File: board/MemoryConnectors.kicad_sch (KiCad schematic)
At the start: 7 parts, among them J29 Conn_02x18_Odd_Even, J30 Conn_02x18_Odd_Even, J31 Conn_02x18_Odd_Even, J32 Conn_02x18_Odd_Even, J33 Conn_02x18_Odd_Even, J34 Conn_02x18_Odd_Even, J35 Conn_02x18_Odd_Even

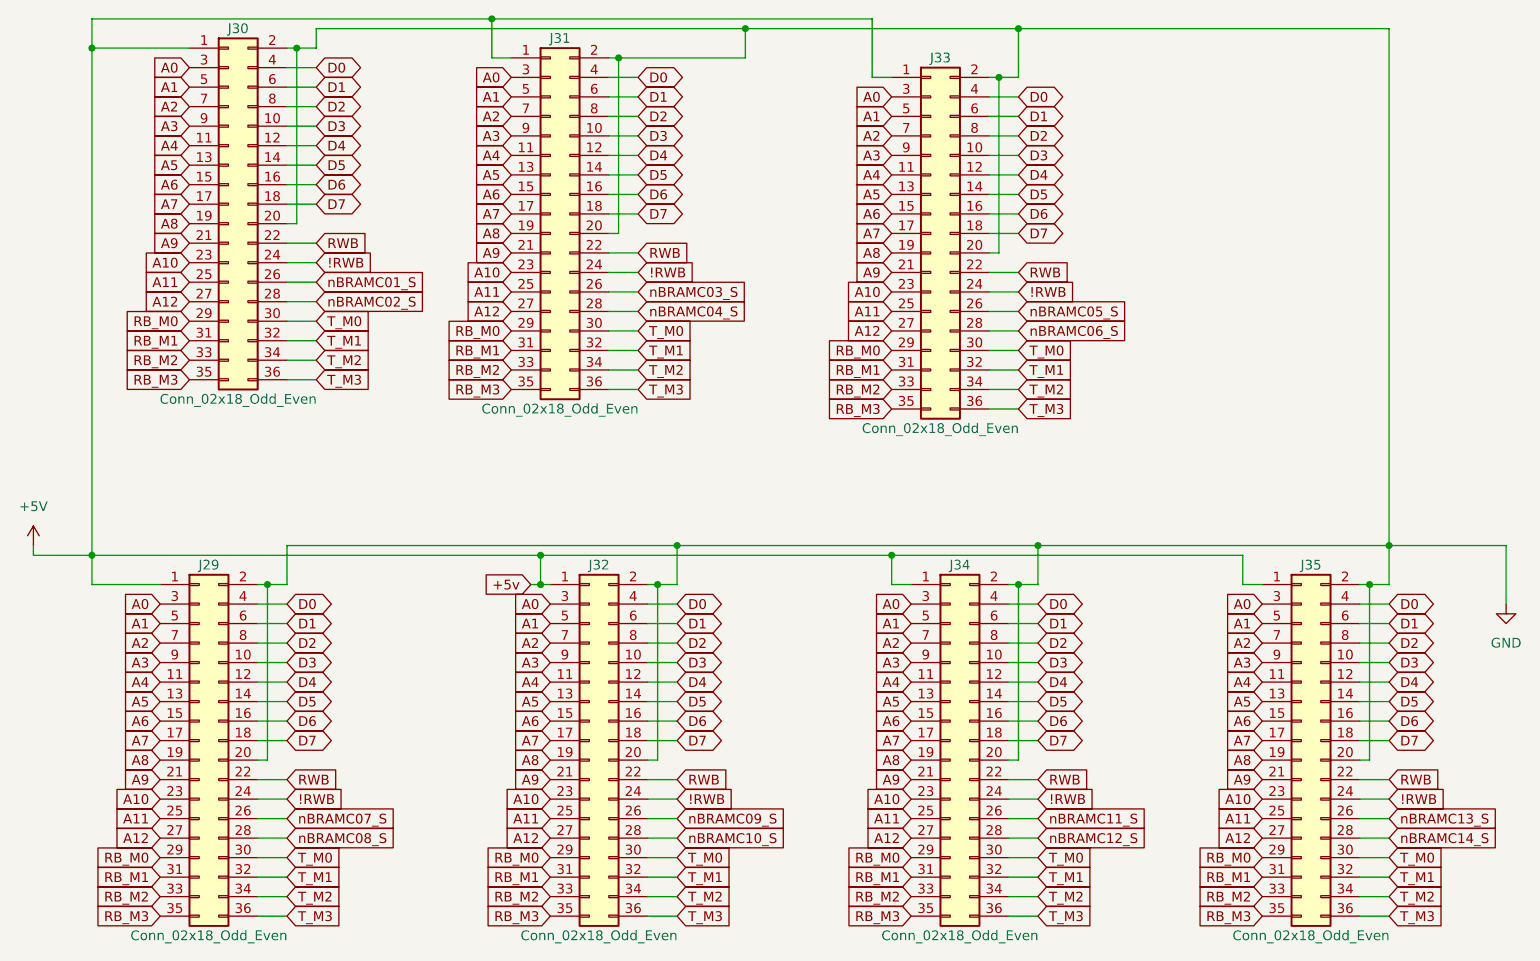
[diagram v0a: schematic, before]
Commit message: V2.0: wait states, GAL glue logic, serial clock and review fixes
Main board schematic:
- Replace the T4-T7 clock divider with RDY wait states. Fixed 7.16 MHz
  CPU clock; J36 selects 3.58 MHz for Rockwell parts. Waits are set per
  region through the write-only register at $FFF5 (reset = 3 waits).
- Move address decode, strobes, the wait-state generator, the IRQ
  encoder/latch/vector mux, ROM bank gating and DMA sync into seven GALs
  (U81-U86 ATF22V10C, U87 ATF16V8C), removing 29 ICs. CUPL sources,
  JEDECs and notes are in board/PLDs/V2.
- 1.8432 MHz serial clock, soft-power latch, -5V regulator, bulk caps,
  pull-ups, audio coupling/decoupling, GNDA tie, read-only Z register
  and other design-review fixes.
- New WaitStates and Support sheets; project symbol library
  hydra16.kicad_sym with sym-lib-table.

PCB updated from the schematic. Includes pending changes to the counter,
bus breakout and memory daughter card projects.

Firmware:
- Remove S_REGISTER; T/U/V/W now at $FFF0-$FFF3 to match the hardware.
- Add math.s and sound.s (included by os_main.s).
- Rebuild the 65C02 ROM image.

Co-Authored-By: Claude Opus 5.5 <noreply@anthropic.com>
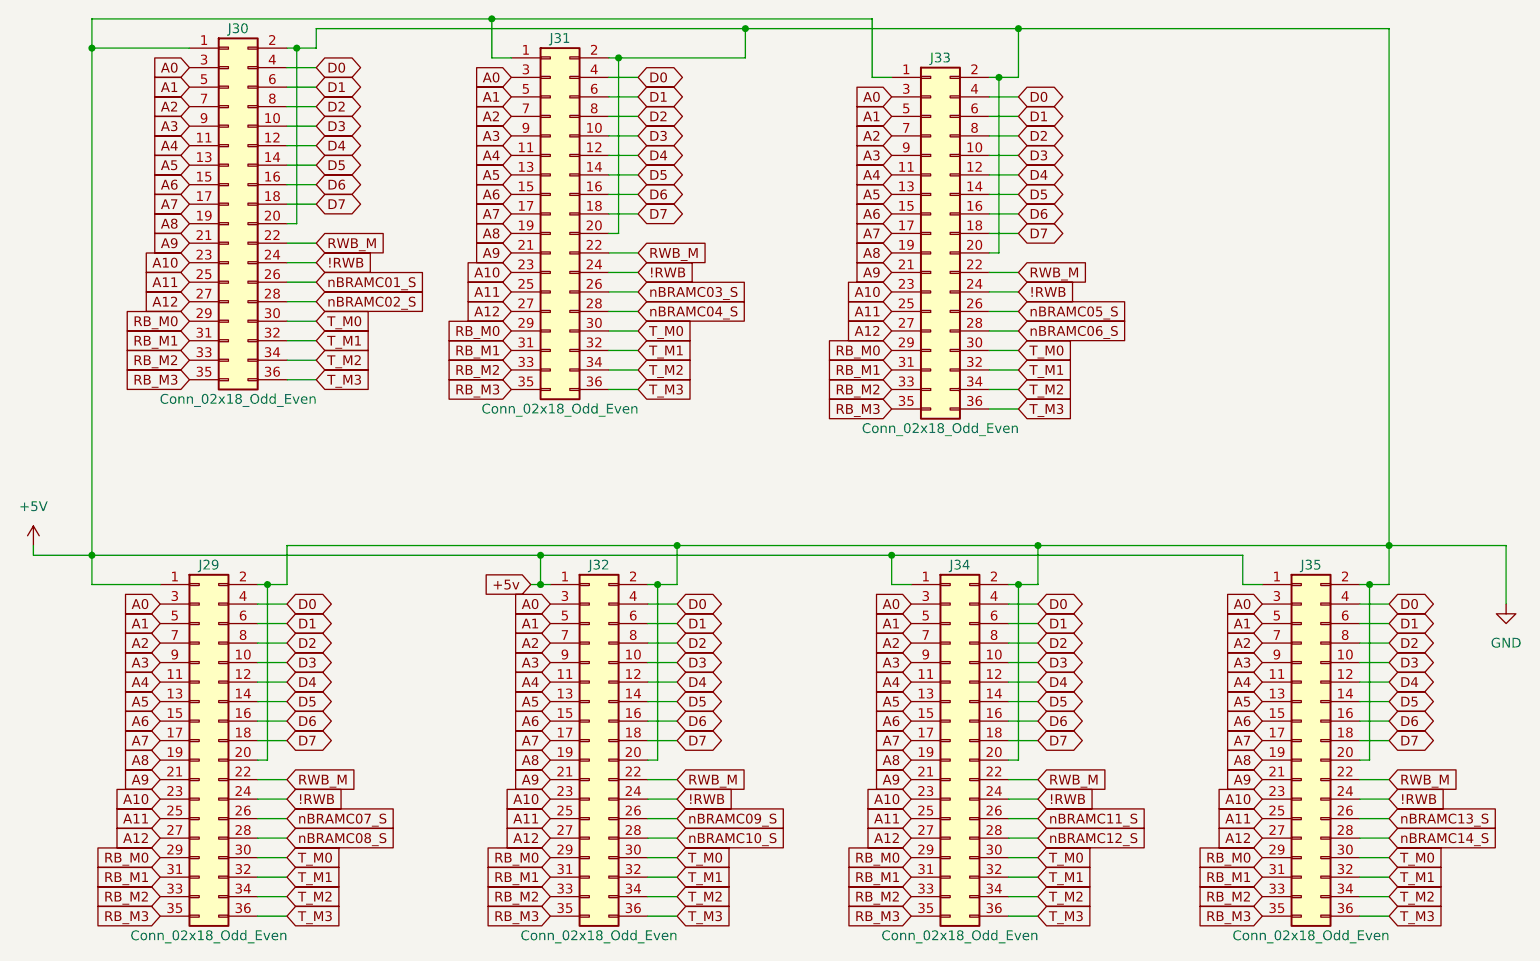
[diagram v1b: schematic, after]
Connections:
- net RWB renamed RWB_M
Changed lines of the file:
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@@
 		)
 	)
-	(global_label "RWB"
+	(global_label "RWB_M"
 		(shape input)
 		(at 113.03 66.04 0)
@@
 		)
 	)
-	(global_label "RWB"
+	(global_label "RWB_M"
 		(shape input)
 		(at 71.12 64.77 0)
@@
 		)
 	)
-	(global_label "RWB"
+	(global_label "RWB_M"
 		(shape input)
 		(at 210.82 134.62 0)
@@
 		)
 	)
-	(global_label "RWB"
+	(global_label "RWB_M"
 		(shape input)
 		(at 118.11 134.62 0)
@@
 		)
 	)
-	(global_label "RWB"
+	(global_label "RWB_M"
 		(shape input)
 		(at 162.56 68.58 0)
@@
 		)
 	)
-	(global_label "RWB"
+	(global_label "RWB_M"
 		(shape input)
 		(at 165.1 134.62 0)
@@
 		)
 	)
-	(global_label "RWB"
+	(global_label "RWB_M"
 		(shape input)
 		(at 67.31 134.62 0)

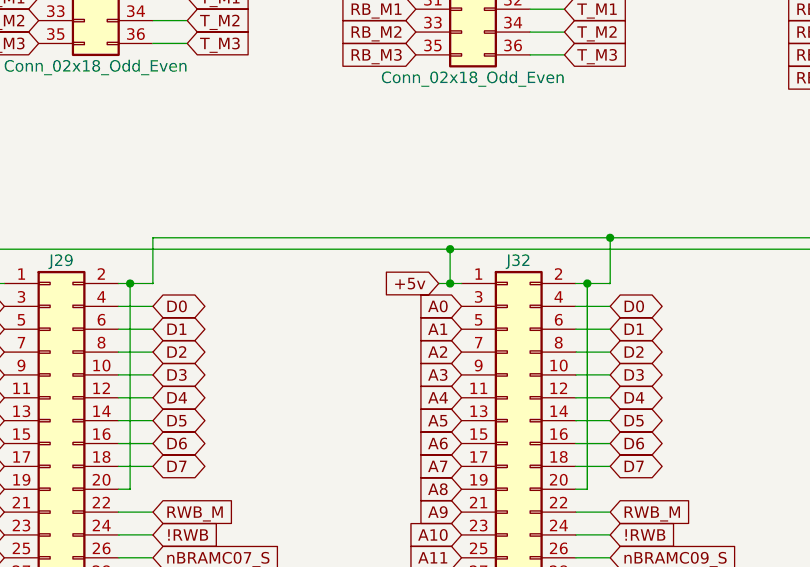
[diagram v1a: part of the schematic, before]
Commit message: V2.0 rev 2.0D: clock stretching, OS ROM paging and review fixes
Bus timing:
- New GAL C (U88) generates PHI2/PHI1 and the 3.58 MHz sound clock from
  the 14.318 MHz master, replacing the U35 74F191 divider. J36 now selects
  7.16 or 3.58 MHz.
- Banked RAM, banked ROM and slot I/O ($FF20-$FFEF) get one extra PHI2-low
  period plus 0-3 extra PHI2-high periods set in $FFF5 (GAL D). This
  replaces the on-board RDY wait generator; cards can still pull RDY.
- Write strobes are now hold-time safe: PHI1 comes straight from GAL C
  and RWB_M straight from GAL B2.

Review fixes:
- OS ROM chip enable from a single-level decode, output enable from
  GAL B1; -55 part specified. Full 4K OS ROM paging via GAL G.
- Vector RAM writes only during PHI2; $FFF0-$FFFF no longer slowed.
- YM2151 /WR on RWB_M. U62 removed. RB0-RB7 pull-ups (RN5).
- Slot clocks driven through U56 and U34 with 33R series resistors.
- J38 enables in-system flashing of the banked ROMs.
- W65C22S/W65C51N, AS6C4008, DS1813-5 and CY7C192-25 values; R4 1k.
- J7 pin 8 no longer +5V; +5VA renamed +5VSB; serial handshake loop.
- Sheet titles and revisions, slot symbol pin fixes, and project symbol
  and footprint libraries so the project opens on another machine.

Co-Authored-By: Claude Opus 5.5 <noreply@anthropic.com>
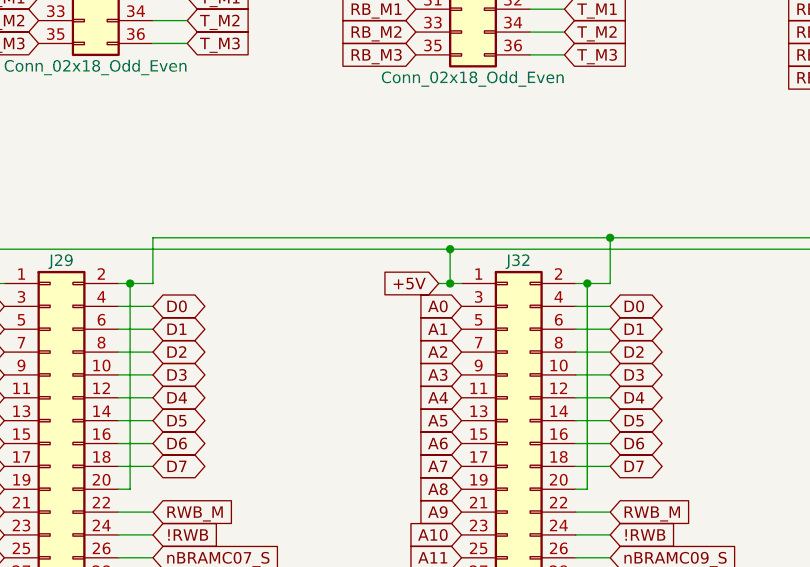
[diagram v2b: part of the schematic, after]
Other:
- title: ZeroPage $00/$01 Mirror Memory and RAM/ROM Bank Logic -> Memory Card Connectors
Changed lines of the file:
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@@
 	(paper "A4")
 	(title_block
-		(title "ZeroPage $00/$01 Mirror Memory and RAM/ROM Bank Logic")
-		(date "2026-01-28")
-		(rev "2.0B")
+		(title "Memory Card Connectors")
+		(date "2026-10-06")
+		(rev "2.0D")
 		(company "Data Tuning")
 		(comment 1 "Hydra 16")
@@
 		)
 	)
-	(global_label "+5v"
+	(global_label "+5V"
 		(shape input)
 		(at 99.06 109.22 180)

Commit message: V2.0: speaker headers, A/D bus fix, layout edits
- On-board speakers LS1/LS2 replaced by 2-pin headers J40 (SPEAKER L)
  and J41 (SPEAKER R) for external mini speakers: pin 1 speaker
  (through R30/R31), pin 2 GNDA; J18 still mutes them
- Connectors: a layout move had joined the A[0..15] and D[0..7] buses
  at two crossings (shorting A0-A7 to D0-D7); buses separated again,
  connectivity matches the previous commit
- Layout edits across the sheets (no other connectivity change)
- PCB updated from the schematic

Co-Authored-By: Claude Opus 5.5 <noreply@anthropic.com>
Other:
- title: Memory Card Connectors -> Expansion Slots, SPI Headers and Port A
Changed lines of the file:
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@@
 	(paper "A4")
 	(title_block
-		(title "Memory Card Connectors")
+		(title "Expansion Slots, SPI Headers and Port A")
 		(date "2026-10-06")
 		(rev "2.0D")
